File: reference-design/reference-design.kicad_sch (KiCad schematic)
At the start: 30 parts

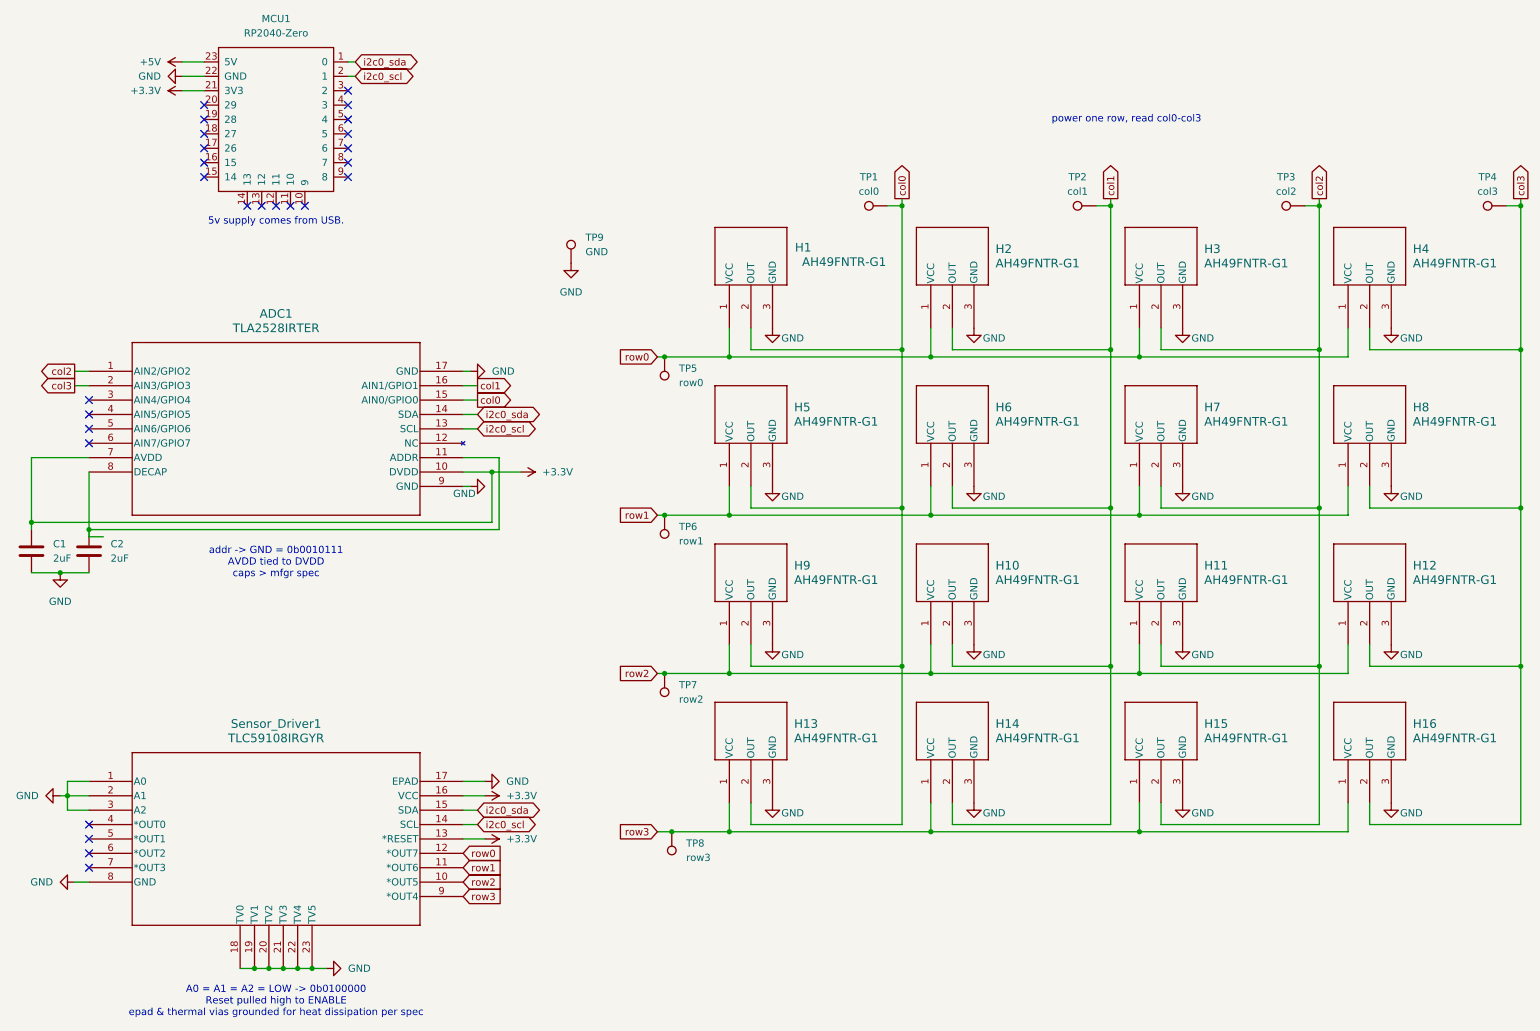
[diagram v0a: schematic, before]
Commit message: replace led driver with another ADC (to be used as gpio to drive MOSFETs)
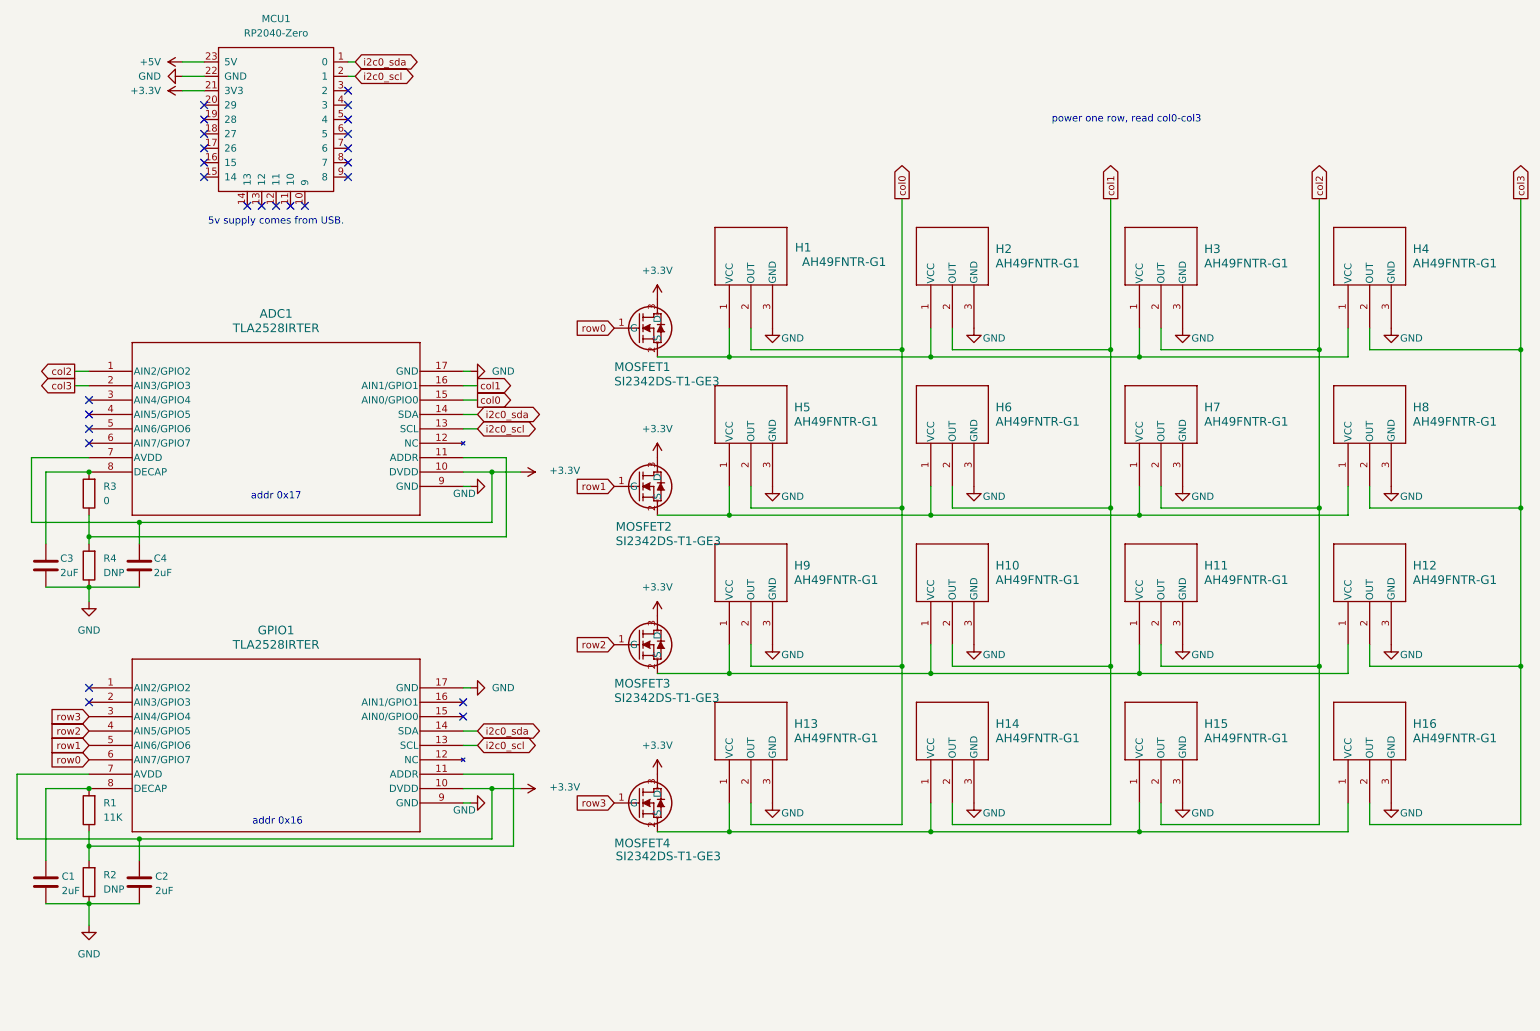
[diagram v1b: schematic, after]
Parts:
- removed Sensor_Driver1: TLC59108IRGYR, TLC59208FIRGYR:RGY16_2P55X2P05, symbol TLC59208FIRGYR:TLC59208FIRGYR
- removed TP1: col0, TestPoint:TestPoint_Pad_2.0x2.0mm, symbol Connector:TestPoint
- removed TP2: col1, TestPoint:TestPoint_Pad_2.0x2.0mm, symbol Connector:TestPoint
- removed TP3: col2, TestPoint:TestPoint_Pad_2.0x2.0mm, symbol Connector:TestPoint
- removed TP4: col3, TestPoint:TestPoint_Pad_2.0x2.0mm, symbol Connector:TestPoint
- removed TP5: row0, TestPoint:TestPoint_Pad_2.0x2.0mm, symbol Connector:TestPoint
- removed TP6: row1, TestPoint:TestPoint_Pad_2.0x2.0mm, symbol Connector:TestPoint
- removed TP7: row2, TestPoint:TestPoint_Pad_2.0x2.0mm, symbol Connector:TestPoint
- removed TP8: row3, TestPoint:TestPoint_Pad_2.0x2.0mm, symbol Connector:TestPoint
- removed TP9: GND, TestPoint:TestPoint_Pad_2.0x2.0mm, symbol Connector:TestPoint
- added C3, C4: 2uF, Capacitor_SMD:C_0603_1608Metric, symbol Device:C
- added GPIO1: TLA2528IRTER, TLA2528IRTER:WQFN16_RTE_TEX, symbol TLA2528IRTER_mod:TLA2528IRTER
- added MOSFET1, MOSFET2, MOSFET3, MOSFET4: SI2342DS-T1-GE3, SI2342DS-T1-GE3:SOT-23_TO-236_VIS, symbol SI2342DS-T1-GE3:SI2342DS-T1-GE3
- added R1: 11K, Resistor_SMD:R_0603_1608Metric, symbol Device:R
- added R2, R4: DNP, Resistor_SMD:R_0603_1608Metric, symbol Device:R
- added R3: 0, Resistor_SMD:R_0603_1608Metric, symbol Device:R
- C1, C2: footprint Capacitor_SMD:C_0805_2012Metric_Pad1.18x1.45mm_HandSolder -> Capacitor_SMD:C_0603_1608Metric
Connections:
- net +3.3V: now also C2.1, C4.1, GPIO1.10 (DVDD), GPIO1.7 (AVDD), MOSFET1.3 (D), MOSFET2.3 (D), MOSFET3.3 (D), MOSFET4.3 (D); no longer C1.1
- net GND: now also C3.2, C4.2, GPIO1.17 (GND), GPIO1.9 (GND), R2.1, R4.1
- net i2c0_scl: now also GPIO1.13 (SCL)
- net i2c0_sda: now also GPIO1.14 (SDA)
- net row0: now also GPIO1.6 (AIN7/GPIO7), MOSFET1.1 (G); no longer H1.1 (VCC), H2.1 (VCC), H3.1 (VCC), H4.1 (VCC)
- net row1: now also GPIO1.5 (AIN6/GPIO6), MOSFET2.1 (G); no longer H5.1 (VCC), H6.1 (VCC), H7.1 (VCC), H8.1 (VCC)
- net row2: now also GPIO1.4 (AIN5/GPIO5), MOSFET3.1 (G); no longer H10.1 (VCC), H11.1 (VCC), H12.1 (VCC), H9.1 (VCC)
- net row3: now also GPIO1.3 (AIN4/GPIO4), MOSFET4.1 (G); no longer H13.1 (VCC), H14.1 (VCC), H15.1 (VCC), H16.1 (VCC)
- new net: H5.1 (VCC), H6.1 (VCC), H7.1 (VCC), H8.1 (VCC), MOSFET2.2 (S)
- new net: H1.1 (VCC), H2.1 (VCC), H3.1 (VCC), H4.1 (VCC), MOSFET1.2 (S)
- new net: H10.1 (VCC), H11.1 (VCC), H12.1 (VCC), H9.1 (VCC), MOSFET3.2 (S)
- new net: H13.1 (VCC), H14.1 (VCC), H15.1 (VCC), H16.1 (VCC), MOSFET4.2 (S)
- new net: ADC1.11 (ADDR), R3.1, R4.2
- new net: C1.1, GPIO1.8 (DECAP), R1.2
- new net: GPIO1.11 (ADDR), R1.1, R2.2
- new net: ADC1.8 (DECAP), C3.1, R3.2
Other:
- note added: "addr 0x16"
- note added: "addr 0x17"
- note removed: "A0 = A1 = A2 = LOW -> 0b0100000 Reset pulled high to ENABLE epad & thermal vias grounded for heat dissipation per spec"
- note removed: "addr -> GND = 0b0010111 AVDD tied to DVDD caps > mfgr spec"
